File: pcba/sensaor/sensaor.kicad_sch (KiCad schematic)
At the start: 18 parts, among them J1 SAO, J12 Conn_01x09_Pin, J13 Conn_01x09_Pin, J2 WS2812, J3 Conn_01x09_Pin, J4 Conn_01x09_Pin, J5 Conn_01x09_Pin, J6 Programming, J7 Speed, J8 Shape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

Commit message: Update PCB
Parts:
- removed J12, J13, J3, J4, J5: Conn_01x09_Pin, Connector_PinHeader_2.54mm:PinHeader_1x09_P2.54mm_Vertical, symbol Connector:Conn_01x09_Pin
- removed J7: Speed, Connector_PinHeader_2.54mm:PinHeader_1x03_P2.54mm_Vertical, symbol Connector:Conn_01x03_Pin
- removed J8: Shape, Connector_PinHeader_2.54mm:PinHeader_1x03_P2.54mm_Vertical, symbol Connector:Conn_01x03_Pin
- removed J9: CONF, Connector_PinHeader_2.54mm:PinHeader_1x03_P2.54mm_Vertical, symbol Connector:Conn_01x03_Pin
- added J3, J4, J5, J7, J8, J9: Conn_01x10_Pin, Connector_PinHeader_2.54mm:PinHeader_1x10_P2.54mm_Vertical, symbol Connector:Conn_01x10_Pin
- J2: footprint Connector_Harwin:Harwin_M20-89003xx_1x03_P2.54mm_Horizontal -> Connector_PinHeader_2.54mm:PinHeader_1x03_P2.54mm_Vertical
- R1, R2: footprint Resistor_SMD:R_0201_0603Metric_Pad0.64x0.40mm_HandSolder -> Capacitor_SMD:C_0402_1005Metric_Pad0.74x0.62mm_HandSolder
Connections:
- net CONF is gone; now on net SHAPE: U1.13 (PA2)
- net AB: now also J9.1 (Pin_1)
- net AG: now also J8.1 (Pin_1)
- net AR: now also J7.1 (Pin_1)
- net GND: now also J4.10 (Pin_10), J7.10 (Pin_10), J9.10 (Pin_10)
- net SHAPE: now also J4.1 (Pin_1); no longer U1.12 (PA1)
- net SPEED: now also J3.1 (Pin_1)
- net VCC: now also J3.10 (Pin_10), J5.10 (Pin_10), J8.10 (Pin_10)
- net LED0 renamed LED
- new net PHASE: J5.1 (Pin_1), U1.12 (PA1)

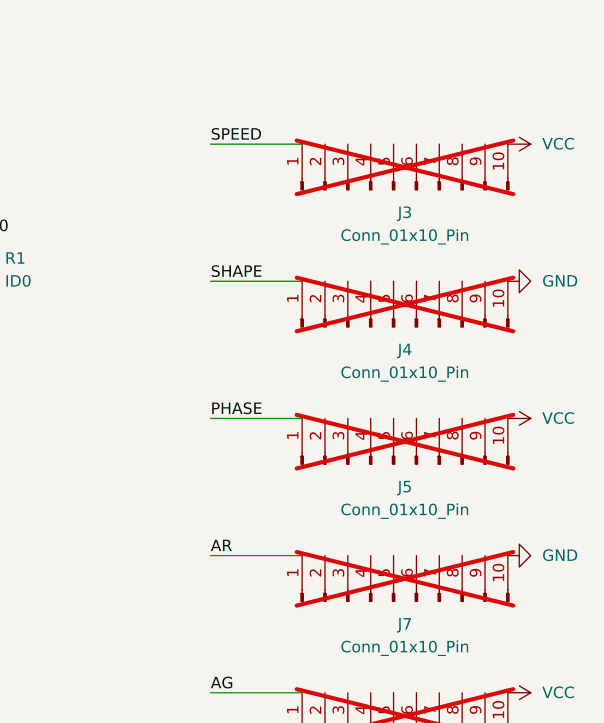
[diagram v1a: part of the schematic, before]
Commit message: Shrink board and fix DRC
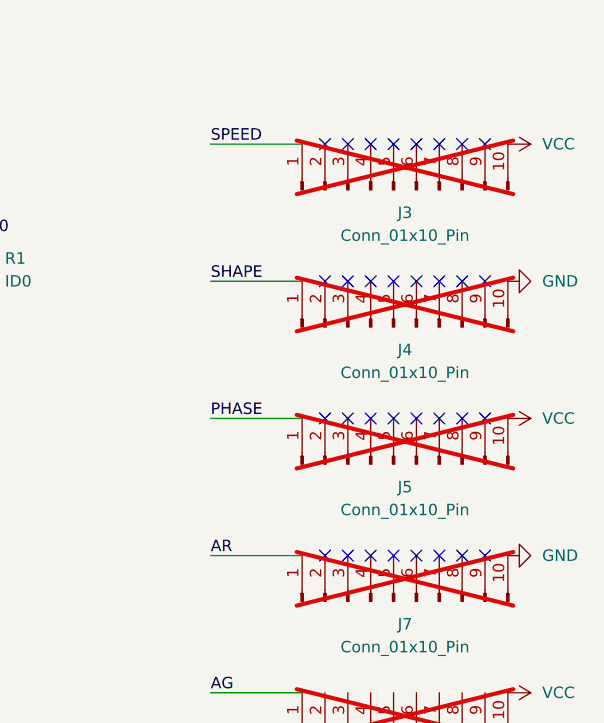
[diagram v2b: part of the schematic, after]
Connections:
- no-connect marks 0 -> 32
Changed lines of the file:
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@@
 	(generator_version "8.0")
 	(paper "A4")
+	(no_connect
+		(at 193.04 80.01)
+	)
+	(no_connect
+		(at 187.96 80.01)
+	)
+	(no_connect
+		(at 195.58 95.25)
+	)
+	(no_connect
+		(at 198.12 80.01)
+	)
+	(no_connect
+		(at 187.96 64.77)
+	)
+	(no_connect
+		(at 193.04 95.25)
+	)
+	(no_connect
+		(at 182.88 49.53)
+	)
+	(no_connect
+		(at 190.5 95.25)
+	)
+	(no_connect
+		(at 187.96 95.25)
+	)
+	(no_connect
+		(at 195.58 80.01)
+	)
+	(no_connect
+		(at 195.58 49.53)
+	)
+	(no_connect
+		(at 195.58 64.77)
+	)
+	(no_connect
+		(at 185.42 64.77)
+	)
+	(no_connect
+		(at 185.42 80.01)
+	)
+	(no_connect
+		(at 190.5 64.77)
+	)
+	(no_connect
+		(at 190.5 80.01)
+	)
+	(no_connect
+		(at 193.04 64.77)
+	)
+	(no_connect
+		(at 182.88 95.25)
+	)
+	(no_connect
+		(at 187.96 49.53)
+	)
+	(no_connect
+		(at 190.5 49.53)
+	)
+	(no_connect
+		(at 185.42 49.53)
+	)
+	(no_connect
+		(at 182.88 80.01)
+	)
+	(no_connect
+		(at 180.34 80.01)
+	)
+	(no_connect
+		(at 180.34 95.25)
+	)
+	(no_connect
+		(at 182.88 64.77)
+	)
+	(no_connect
+		(at 193.04 49.53)
+	)
+	(no_connect
+		(at 198.12 49.53)
+	)
+	(no_connect
+		(at 180.34 49.53)
+	)
+	(no_connect
+		(at 198.12 64.77)
+	)
+	(no_connect
+		(at 180.34 64.77)
+	)
+	(no_connect
+		(at 185.42 95.25)
+	)
+	(no_connect
+		(at 198.12 95.25)
+	)
 	(wire
 		(pts

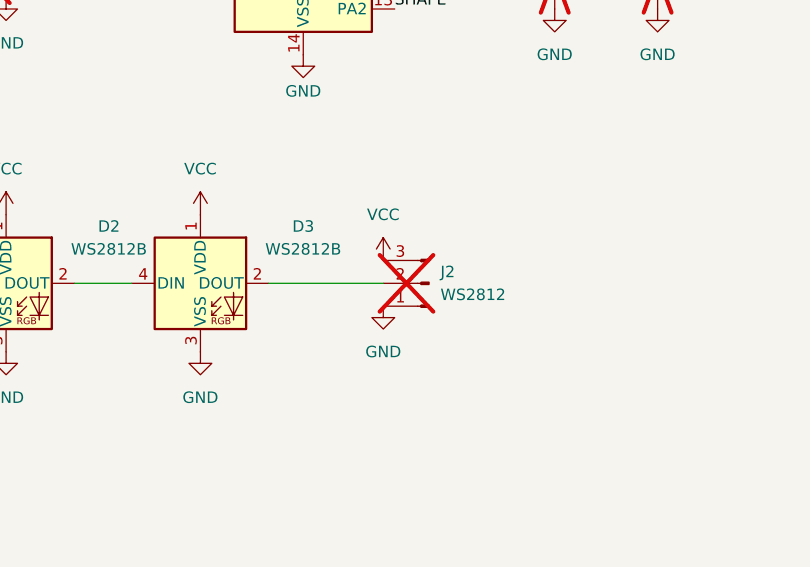
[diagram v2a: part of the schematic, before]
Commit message: Add ground pours, update silkscreen
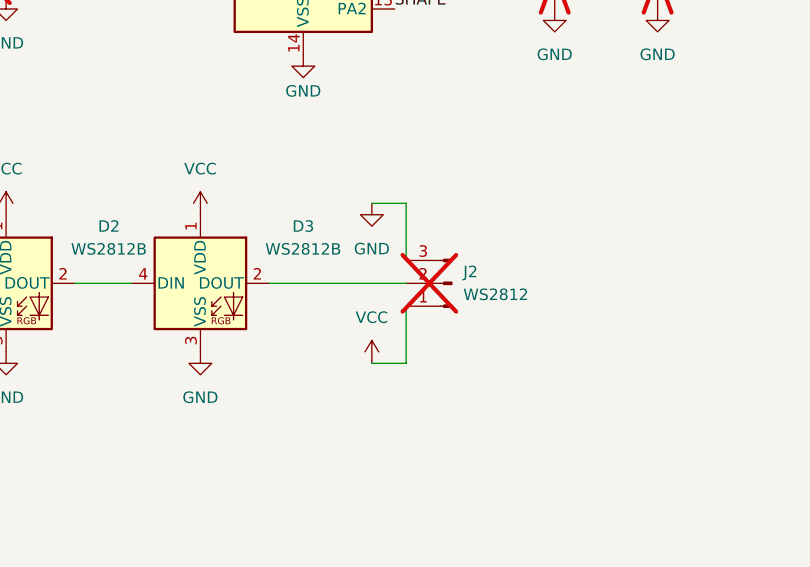
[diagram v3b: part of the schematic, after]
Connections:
- net GND: now also J2.3 (Pin_3); no longer J2.1 (Pin_1)
- net VCC: now also J2.1 (Pin_1); no longer J2.3 (Pin_3)
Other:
- moved on the sheet: J2
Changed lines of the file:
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@@
+	(wire
+		(pts
+			(xy 114.3 106.68) (xy 114.3 100.33)
+		)
+		(stroke
+			(width 0)
+			(type default)
+		)
+	)
 	(wire
 		(pts
@@
 	(wire
 		(pts
-			(xy 86.36 52.07) (xy 92.71 52.07)
+			(xy 99.06 97.79) (xy 114.3 97.79)
 		)
 		(stroke
@@
 	(wire
 		(pts
-			(xy 38.1 49.53) (xy 44.45 49.53)
+			(xy 86.36 52.07) (xy 92.71 52.07)
 		)
 		(stroke
@@
 	(wire
 		(pts
-			(xy 167.64 64.77) (xy 177.8 64.77)
+			(xy 38.1 49.53) (xy 44.45 49.53)
 		)
 		(stroke
@@
 	(wire
 		(pts
-			(xy 99.06 97.79) (xy 111.76 97.79)
+			(xy 167.64 64.77) (xy 177.8 64.77)
 		)
 		(stroke
@@
 	(wire
 		(pts
-			(xy 167.64 95.25) (xy 177.8 95.25)
+			(xy 114.3 88.9) (xy 114.3 95.25)
 		)
 		(stroke
@@
 	(wire
 		(pts
-			(xy 86.36 59.69) (xy 92.71 59.69)
+			(xy 167.64 95.25) (xy 177.8 95.25)
 		)
 		(stroke
@@
 	(wire
 		(pts
-			(xy 167.64 49.53) (xy 177.8 49.53)
+			(xy 86.36 59.69) (xy 92.71 59.69)
 		)
 		(stroke
@@
 	(wire
 		(pts
-			(xy 53.34 97.79) (xy 62.23 97.79)
+			(xy 167.64 49.53) (xy 177.8 49.53)
 		)
 		(stroke
@@
 	(wire
 		(pts
-			(xy 38.1 46.99) (xy 44.45 46.99)
+			(xy 53.34 97.79) (xy 62.23 97.79)
 		)
 		(stroke
@@
 	(wire
 		(pts
-			(xy 86.36 57.15) (xy 92.71 57.15)
+			(xy 38.1 46.99) (xy 44.45 46.99)
 		)
 		(stroke
@@
 	(wire
 		(pts
-			(xy 86.36 62.23) (xy 92.71 62.23)
+			(xy 110.49 88.9) (xy 114.3 88.9)
 		)
 		(stroke
@@
 	(wire
 		(pts
-			(xy 86.36 54.61) (xy 92.71 54.61)
+			(xy 86.36 57.15) (xy 92.71 57.15)
 		)
 		(stroke
@@
 	(wire
 		(pts
-			(xy 86.36 49.53) (xy 92.71 49.53)
+			(xy 86.36 62.23) (xy 92.71 62.23)
 		)
 		(stroke
@@
 	(wire
 		(pts
-			(xy 86.36 46.99) (xy 92.71 46.99)
+			(xy 86.36 54.61) (xy 92.71 54.61)
 		)
 		(stroke
@@
 		)
 	)
+	(wire
+		(pts
+			(xy 86.36 49.53) (xy 92.71 49.53)
+		)
+		(stroke
+			(width 0)
+			(type default)
+		)
+	)
+	(wire
+		(pts
+			(xy 110.49 106.68) (xy 114.3 106.68)
+		)
+		(stroke
+			(width 0)
+			(type default)
+		)
+	)
+	(wire
+		(pts
+			(xy 86.36 46.99) (xy 92.71 46.99)
+		)
+		(stroke
+			(width 0)
+			(type default)
+		)
+	)
 	(label "AG"
 		(at 167.64 110.49 0)
@@
 	(symbol
 		(lib_id "power:VCC")
-		(at 111.76 95.25 0)
+		(at 110.49 106.68 0)
 		(unit 1)
 		(exclude_from_sim no)
@@
 		(fields_autoplaced yes)
 		(property "Reference" "#PWR013"
-			(at 111.76 99.06 0)
+			(at 110.49 110.49 0)
 			(effects
 				(font
@@
 		)
 		(property "Value" "VCC"
-			(at 111.76 90.17 0)
+			(at 110.49 101.6 0)
 			(effects
 				(font
@@
 		)
 		(property "Footprint" ""
-			(at 111.76 95.25 0)
+			(at 110.49 106.68 0)
 			(effects
 				(font
@@
 		)
 		(property "Datasheet" ""
-			(at 111.76 95.25 0)
+			(at 110.49 106.68 0)
 			(effects
 				(font
@@
 		)
 		(property "Description" "Power symbol creates a global label with name \"VCC\""
-			(at 111.76 95.25 0)
+			(at 110.49 106.68 0)
 			(effects
 				(font
@@
 	(symbol
 		(lib_id "Connector:Conn_01x03_Pin")
-		(at 116.84 97.79 180)
+		(at 119.38 97.79 180)
 		(unit 1)
 		(exclude_from_sim no)
@@
 		(fields_autoplaced yes)
 		(property "Reference" "J2"
-			(at 118.11 96.5199 0)
+			(at 120.65 96.5199 0)
 			(effects
 				(font
@@
 		)
 		(property "Value" "WS2812"
-			(at 118.11 99.0599 0)
+			(at 120.65 99.0599 0)
 			(effects
 				(font
@@
 		)
 		(property "Footprint" "Connector_PinHeader_2.54mm:PinHeader_1x03_P2.54mm_Vertical"
-			(at 116.84 97.79 0)
+			(at 119.38 97.79 0)
 			(effects
 				(font
@@
 		)
 		(property "Datasheet" "~"
-			(at 116.84 97.79 0)
+			(at 119.38 97.79 0)
 			(effects
 				(font
@@
 		)
 		(property "Description" "Generic connector, single row, 01x03, script generated"
-			(at 116.84 97.79 0)
+			(at 119.38 97.79 0)
 			(effects
 				(font
@@
 	(symbol
 		(lib_id "power:GND")
-		(at 111.76 100.33 0)
+		(at 110.49 88.9 0)
 		(unit 1)
 		(exclude_from_sim no)
@@
 		(fields_autoplaced yes)
 		(property "Reference" "#PWR014"
-			(at 111.76 106.68 0)
+			(at 110.49 95.25 0)
 			(effects
 				(font
@@
 		)
 		(property "Value" "GND"
-			(at 111.76 105.41 0)
+			(at 110.49 93.98 0)
 			(effects
 				(font
@@
 		)
 		(property "Footprint" ""
-			(at 111.76 100.33 0)
+			(at 110.49 88.9 0)
 			(effects
 				(font
@@
 		)
 		(property "Datasheet" ""
-			(at 111.76 100.33 0)
+			(at 110.49 88.9 0)
 			(effects
 				(font
@@
 		)
 		(property "Description" "Power symbol creates a global label with name \"GND\" , ground"
-			(at 111.76 100.33 0)
-			(effects
-				(font
+			(at 110.49 88.9 0)
+			(effects
+				(font

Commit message: Moving some traces
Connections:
- net AG: now also U1.9 (PD5); no longer U1.10 (PD6)
- net AR: now also U1.10 (PD6); no longer U1.9 (PD5)
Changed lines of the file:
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@@
 		)
 	)
-	(label "AR"
+	(label "AG"
 		(at 113.03 52.07 0)
 		(fields_autoplaced yes)
@@
 		)
 	)
-	(label "AG"
+	(label "AR"
 		(at 113.03 54.61 0)
 		(fields_autoplaced yes)

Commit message: Updates from review feedback, shrunk board more
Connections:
- net GPIO2: now also U1.16 (PC0); no longer U1.6 (PC7)
- net ID0: now also U1.6 (PC7); no longer U1.16 (PC0)
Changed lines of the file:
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@@
 		)
 	)
-	(label "GPIO2"
+	(label "ID0"
 		(at 86.36 62.23 0)
 		(fields_autoplaced yes)
@@
 		)
 	)
-	(label "ID0"
+	(label "GPIO2"
 		(at 86.36 46.99 0)
 		(fields_autoplaced yes)

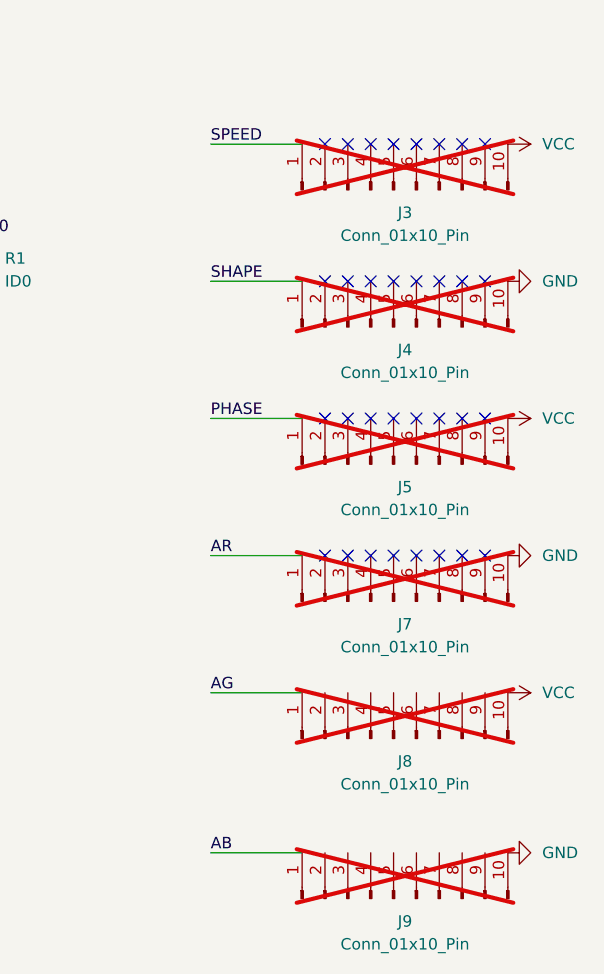
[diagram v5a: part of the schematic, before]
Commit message: Redesign board into more of a carrier shape
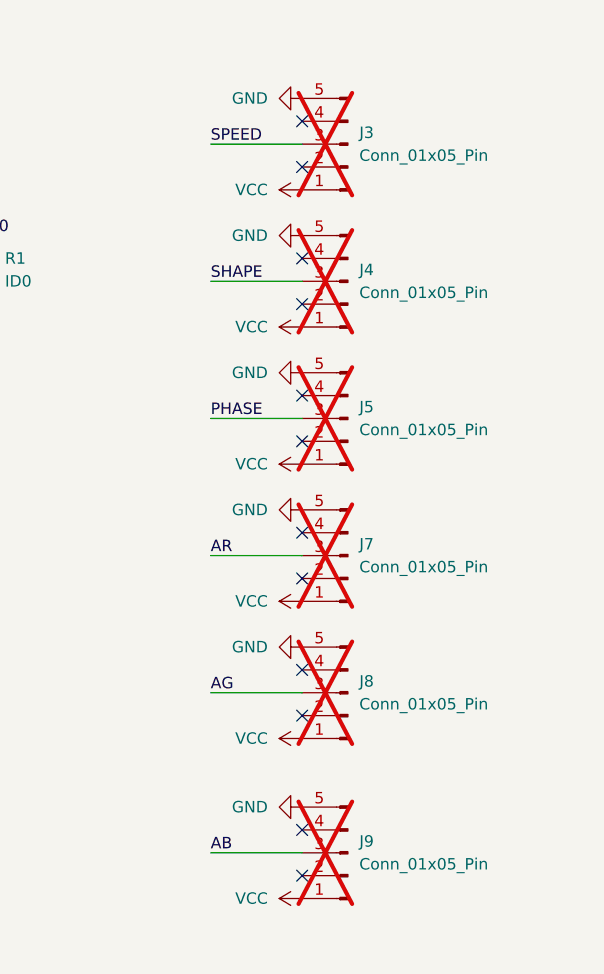
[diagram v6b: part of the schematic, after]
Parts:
- removed J3, J4, J5, J7, J8, J9: Conn_01x10_Pin, Connector_PinHeader_2.54mm:PinHeader_1x10_P2.54mm_Vertical, symbol Connector:Conn_01x10_Pin
- added J3, J4, J5, J7, J8, J9: Conn_01x05_Pin, Connector_PinHeader_2.54mm:PinHeader_1x05_P2.54mm_Vertical, symbol Connector:Conn_01x05_Pin
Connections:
- net AB: now also J9.3 (Pin_3)
- net AG: now also J8.3 (Pin_3)
- net AR: now also J7.3 (Pin_3)
- net GND: now also J3.5 (Pin_5), J4.5 (Pin_5), J5.5 (Pin_5), J7.5 (Pin_5), J8.5 (Pin_5), J9.5 (Pin_5)
- net PHASE: now also J5.3 (Pin_3)
- net SHAPE: now also J4.3 (Pin_3)
- net SPEED: now also J3.3 (Pin_3)
- net VCC: now also J3.1 (Pin_1), J4.1 (Pin_1), J5.1 (Pin_1), J7.1 (Pin_1), J8.1 (Pin_1), J9.1 (Pin_1)
- no-connect marks 32 -> 12

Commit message: Add SAOAO connector, tweak some placements
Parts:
- added J10: SAOAO, Connector_PinHeader_1.27mm:PinHeader_1x03_P1.27mm_Vertical, symbol Connector:Conn_01x03_Socket
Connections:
- net GND: now also J10.1 (Pin_1), J10.3 (Pin_3)
- net VCC: now also J10.2 (Pin_2)
